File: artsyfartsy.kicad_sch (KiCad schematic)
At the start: 29 parts, among them J1 Conn_01x02_Male, SW1 SW_Push, SW11 SW_Push_SPDT, SW12 SW_Push_SPDT, SW2 SW_Push, SW3 SW_Push, SW4 SW_Push, SW5 SW_Push, SW6 SW_Push, SW7 SW_Push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

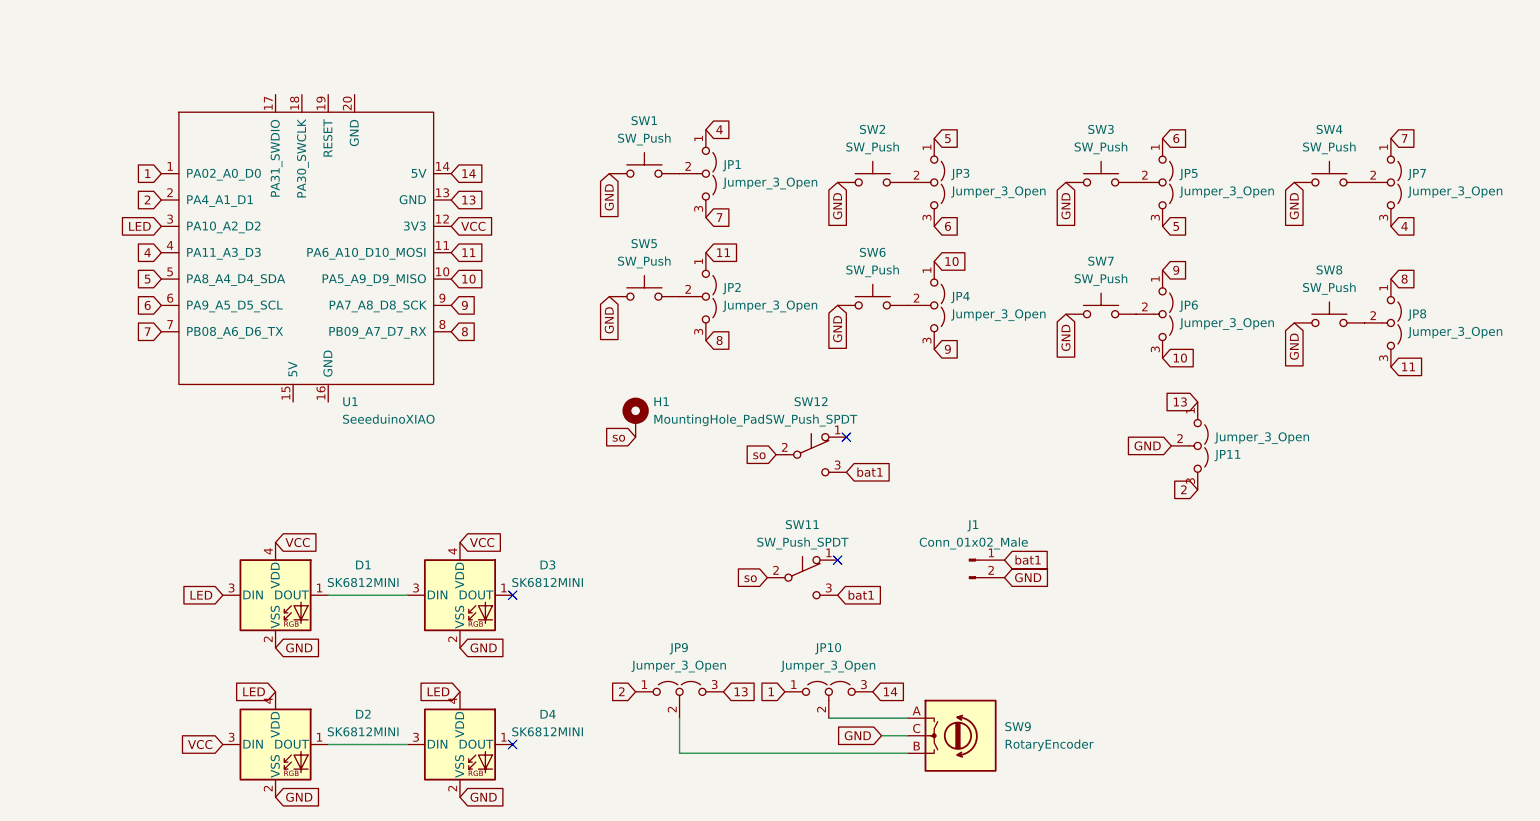
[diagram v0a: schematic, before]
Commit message: updated service hole fot battery
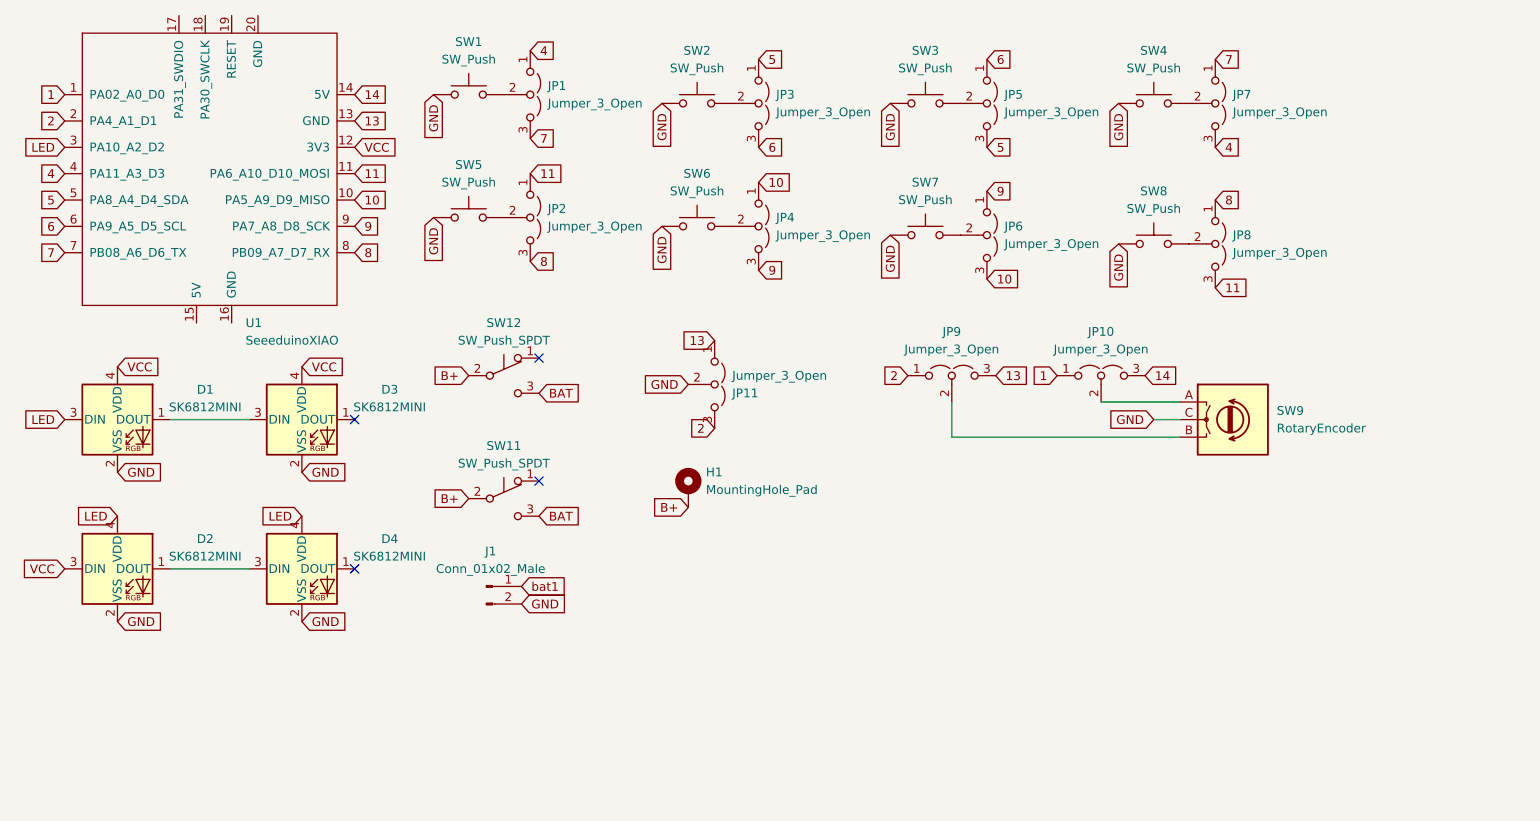
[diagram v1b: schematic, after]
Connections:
- net bat1: no longer SW11.3 (C), SW12.3 (C)
- net so renamed B+
- new net BAT: SW11.3 (C), SW12.3 (C)
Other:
- moved on the sheet: D1, D2, D3, D4, H1, J1, JP1, JP10, JP11, JP2, JP3, JP4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
